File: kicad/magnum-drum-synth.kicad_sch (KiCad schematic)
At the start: 127 parts, among them J1 Piezo, J10 Conn_01x04_Header, J11 Conn_01x04_Socket, J12 Eurorack Mono Jack, J18 Eurorack Mono Jack, J2 Eurorack Mono Jack, J20 Conn_01x02_Socket, J21 Conn_01x02_Header, J22 Conn_01x02_Header, J23 Conn_01x02_Socket, J26 Eurorack Mono Jack, J3 Conn_01x04_Socket, J4 Conn_01x04_Header, J5 Conn_01x03_Header, J6 Conn_01x06_Header, J7 Conn_01x06_Socket, J8 Conn_01x06_Header, J9 Conn_01x06_Socket, Q1 2N3904, Q2 2N3904, Q3 2N3904, Q4 2N3904, Q5 2N3904, Q6 2N3906, Q7 2N3906, Q8 2N3906, Q9 2N3906, SW1 DPDT, U1 CD4093, U2 TL072, U3 TL072, U4 TL074, U7 LM13700

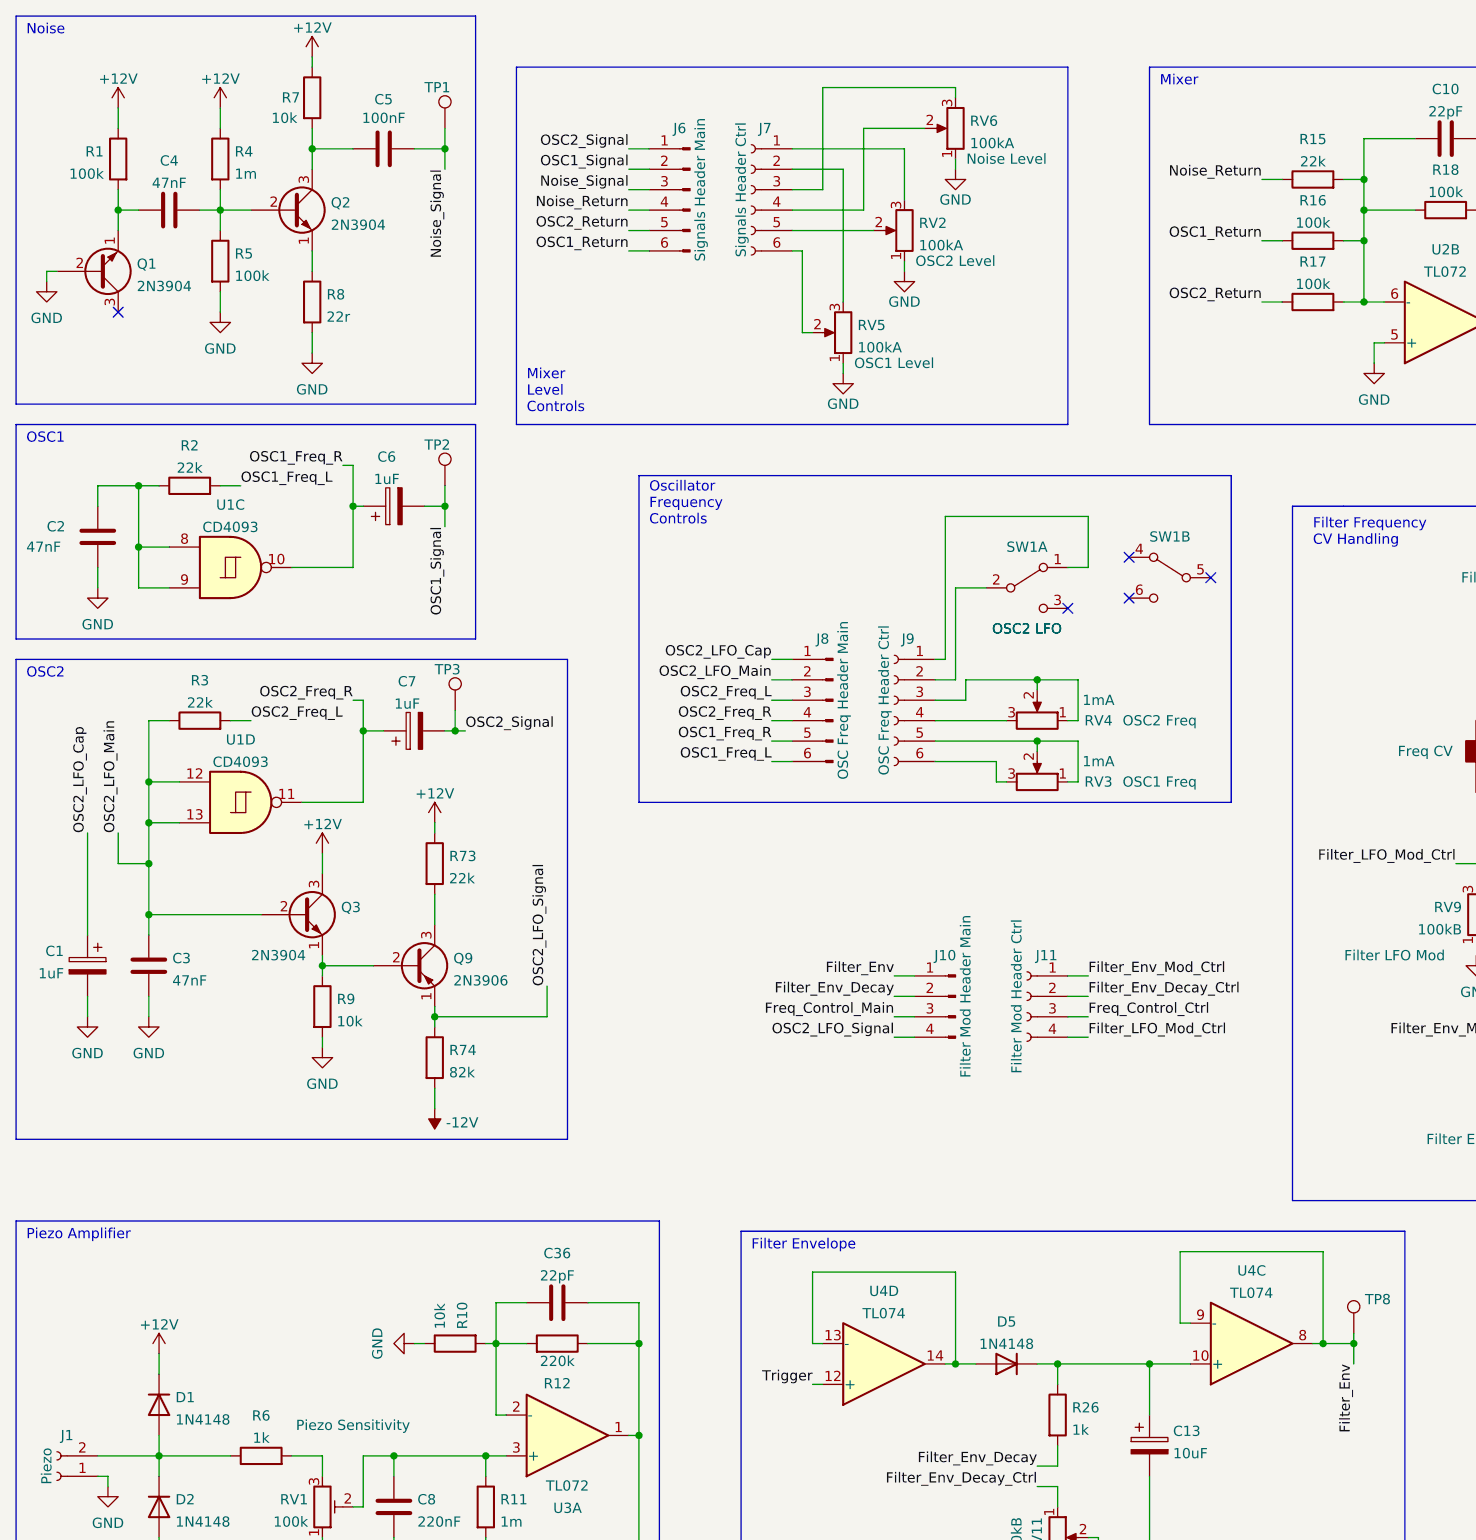
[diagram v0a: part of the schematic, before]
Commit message: Tweaking schematic and bom values
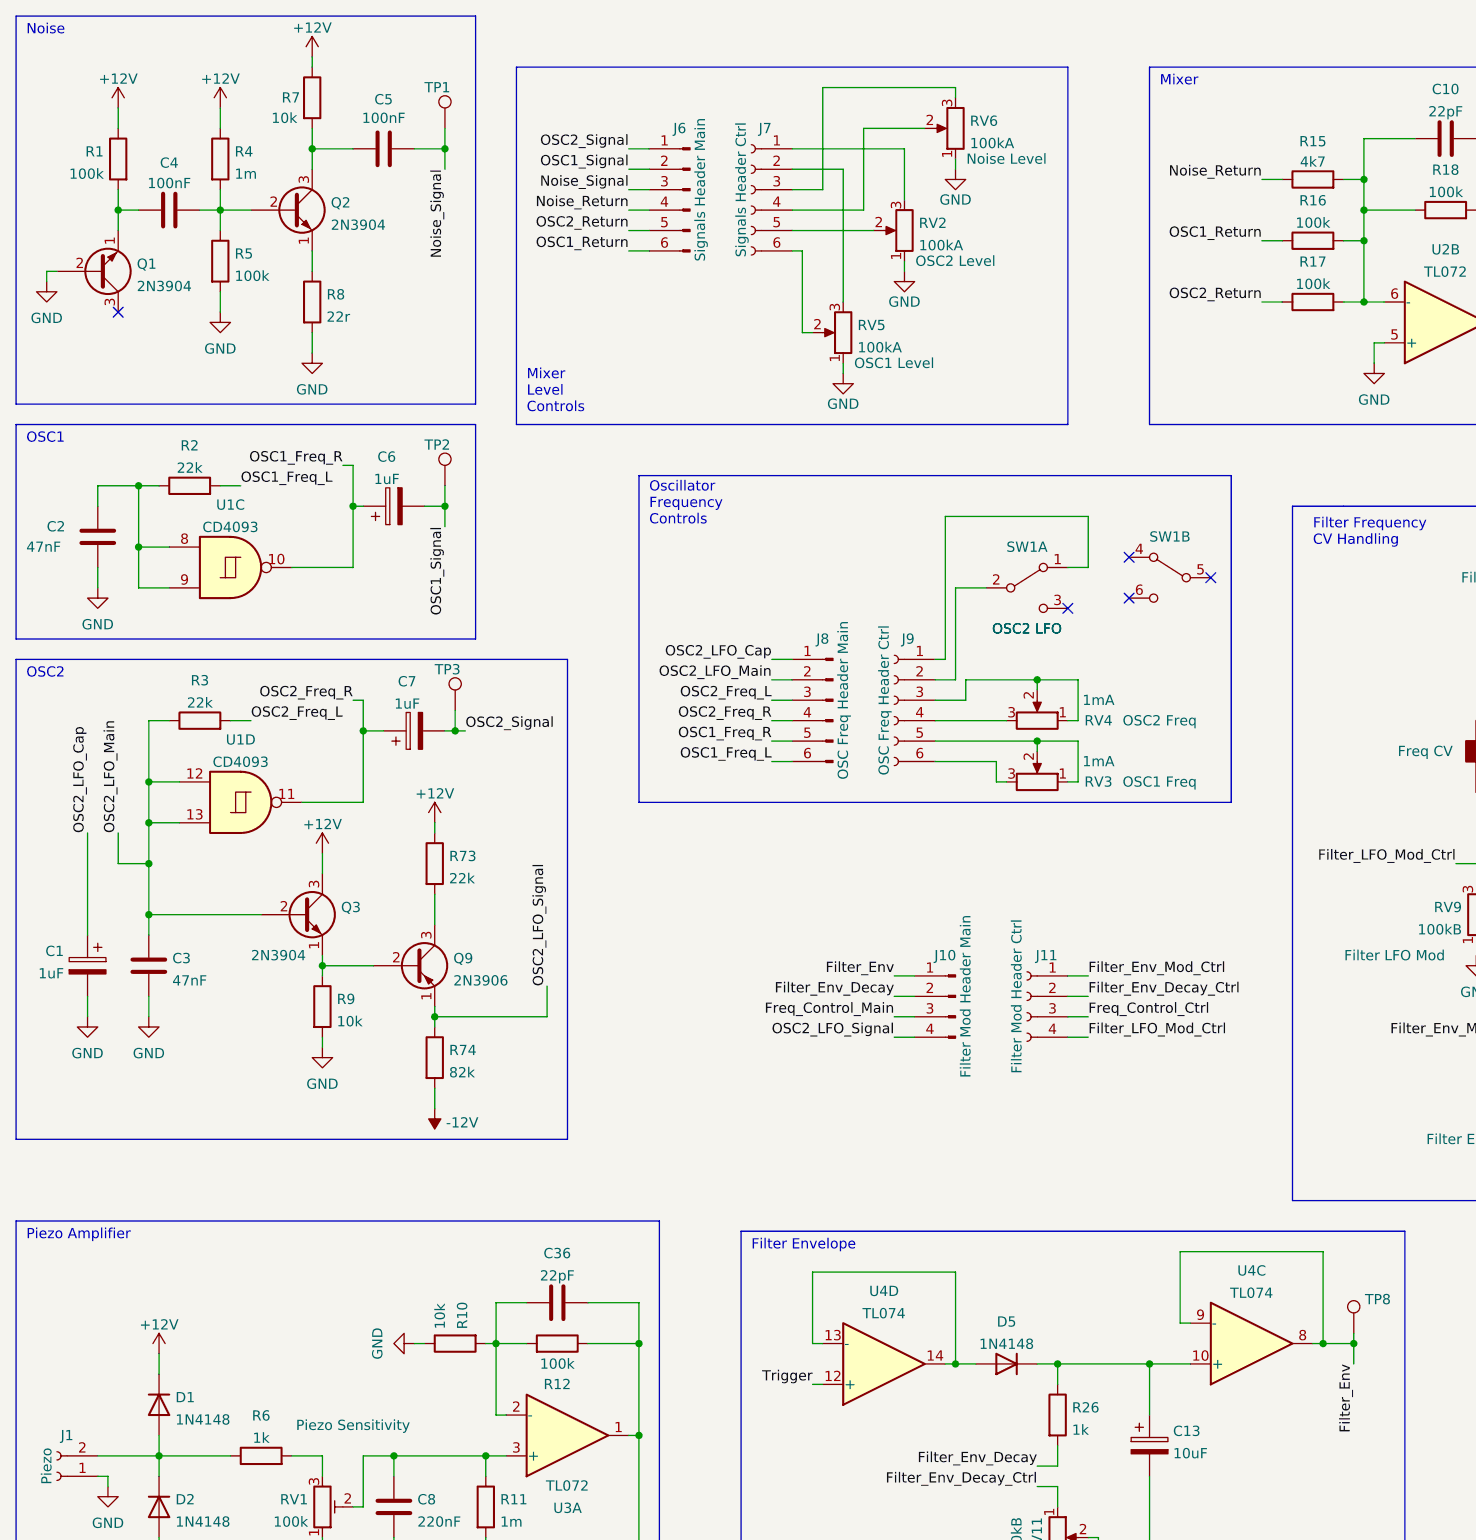
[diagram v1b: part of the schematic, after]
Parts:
- C4: value 47nF -> 100nF; Spec ceramic C0G -> ceramic X7R
- C8: Spec ceramic C0G -> ceramic X7R
- R12: value 220k -> 100k
- R15: value 22k -> 4k7
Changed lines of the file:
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@@
   (symbol (lib_id "Device:R") (at 175.26 34.29 90) (unit 1)
     (in_bom yes) (on_board yes) (fields_autoplaced)
-    (property "Reference" "R15" (id 0) (at 175.26 29.3075 90))
-    (property "Value" "22k" (id 1) (at 175.26 32.0826 90))
+    (property "Reference" "R15" (id 0) (at 175.26 29.5742 90))
+    (property "Value" "4k7" (id 1) (at 175.26 32.1111 90))
     (property "Footprint" "rumblesan-standard-parts:R_Axial_DIN0207_L6.3mm_D2.5mm_P10.16mm_Horizontal" (id 2) (at 175.26 36.068 90)
       (effects (font (size 1.27 1.27)) hide)
@@
   (symbol (lib_id "Device:C") (at 33.02 38.1 90) (unit 1)
     (in_bom yes) (on_board yes) (fields_autoplaced)
-    (property "Reference" "C4" (id 0) (at 33.02 31.9745 90))
-    (property "Value" "47nF" (id 1) (at 33.02 34.7496 90))
+    (property "Reference" "C4" (id 0) (at 33.02 32.2412 90))
+    (property "Value" "100nF" (id 1) (at 33.02 34.7781 90))
     (property "Footprint" "rumblesan-standard-parts:C_Rect_L7.0mm_W3.5mm_P5.00mm" (id 2) (at 36.83 37.1348 0)
       (effects (font (size 1.27 1.27)) hide)
@@
       (effects (font (size 1.27 1.27)) hide)
     )
-    (property "Spec" "ceramic C0G" (id 4) (at 33.02 38.1 0)
+    (property "Spec" "ceramic X7R" (id 4) (at 33.02 38.1 0)
       (effects (font (size 1.27 1.27)) hide)
     )
@@
       (effects (font (size 1.27 1.27)) hide)
     )
-    (property "Spec" "ceramic C0G" (id 4) (at 60.96 199.39 0)
+    (property "Spec" "ceramic X7R" (id 4) (at 60.96 199.39 0)
       (effects (font (size 1.27 1.27)) hide)
     )
@@
   )
   (symbol (lib_id "Device:R") (at 81.28 179.07 270) (mirror x) (unit 1)
-    (in_bom yes) (on_board yes) (fields_autoplaced)
-    (property "Reference" "R12" (id 0) (at 81.28 184.0525 90))
-    (property "Value" "220k" (id 1) (at 81.28 181.2774 90))
+    (in_bom yes) (on_board yes)
+    (property "Reference" "R12" (id 0) (at 81.28 184.15 90))
+    (property "Value" "100k" (id 1) (at 81.28 181.61 90))
     (property "Footprint" "rumblesan-standard-parts:R_Axial_DIN0207_L6.3mm_D2.5mm_P10.16mm_Horizontal" (id 2) (at 81.28 180.848 90)
       (effects (font (size 1.27 1.27)) hide)
@@
     )
     (path "/8591861f-2b7e-410e-8cfd-e20f7fcb6cbb"
-      (reference "C4") (unit 1) (value "47nF") (footprint "rumblesan-standard-parts:C_Rect_L7.0mm_W3.5mm_P5.00mm")
+      (reference "C4") (unit 1) (value "100nF") (footprint "rumblesan-standard-parts:C_Rect_L7.0mm_W3.5mm_P5.00mm")
     )
     (path "/0de452c1-c2d3-4d1a-b78a-15cceb3751d2"
@@
     )
     (path "/ad4c3087-473c-478a-8ad4-a1491b332c93/8e05464c-6ddb-45f0-a810-9a3b853897d8"
-      (reference "C21") (unit 1) (value "1uF") (footprint "rumblesan-standard-parts:CP_Radial_D5.0mm_P2.00mm")
+      (reference "C21") (unit 1) (value "10uF") (footprint "rumblesan-standard-parts:CP_Radial_D5.0mm_P2.00mm")
     )
     (path "/ad4c3087-473c-478a-8ad4-a1491b332c93/09fde542-3167-43f5-a315-cf966de10fd0"
-      (reference "C22") (unit 1) (value "1uF") (footprint "rumblesan-standard-parts:CP_Radial_D5.0mm_P2.00mm")
+      (reference "C22") (unit 1) (value "10uF") (footprint "rumblesan-standard-parts:CP_Radial_D5.0mm_P2.00mm")
     )
     (path "/ad4c3087-473c-478a-8ad4-a1491b332c93/e7127e9e-59ba-43a9-9501-cbea73a5bb0a"
@@
     )
     (path "/963dd436-ddf3-4162-9f66-c28717ca731d"
-      (reference "R12") (unit 1) (value "220k") (footprint "rumblesan-standard-parts:R_Axial_DIN0207_L6.3mm_D2.5mm_P10.16mm_Horizontal")
+      (reference "R12") (unit 1) (value "100k") (footprint "rumblesan-standard-parts:R_Axial_DIN0207_L6.3mm_D2.5mm_P10.16mm_Horizontal")
     )
     (path "/551bcd8e-03fa-4a5d-a22b-e038948336fc"
@@
     )
     (path "/33c83fc5-c4d0-450d-8557-408764e81e50"
-      (reference "R15") (unit 1) (value "22k") (footprint "rumblesan-standard-parts:R_Axial_DIN0207_L6.3mm_D2.5mm_P10.16mm_Horizontal")
+      (reference "R15") (unit 1) (value "4k7") (footprint "rumblesan-standard-parts:R_Axial_DIN0207_L6.3mm_D2.5mm_P10.16mm_Horizontal")
     )
     (path "/2eeac2dd-822d-48a2-8f8a-2fe3eb0d1b17"
@@
     )
     (path "/32f36dff-8662-485b-aca6-8ee96ddb3fbd/06d71e33-f77c-4bc4-8a4f-6532c1f037b7"
-      (reference "R71") (unit 1) (value "33k") (footprint "rumblesan-standard-parts:R_Axial_DIN0207_L6.3mm_D2.5mm_P10.16mm_Horizontal")
+      (reference "R71") (unit 1) (value "68k") (footprint "rumblesan-standard-parts:R_Axial_DIN0207_L6.3mm_D2.5mm_P10.16mm_Horizontal")
     )
     (path "/32f36dff-8662-485b-aca6-8ee96ddb3fbd/4a39f7d1-4843-4924-b280-b77be7d7ddd6"
-      (reference "R72") (unit 1) (value "10k") (footprint "rumblesan-standard-parts:R_Axial_DIN0207_L6.3mm_D2.5mm_P10.16mm_Horizontal")
+      (reference "R72") (unit 1) (value "33k") (footprint "rumblesan-standard-parts:R_Axial_DIN0207_L6.3mm_D2.5mm_P10.16mm_Horizontal")
     )
     (path "/c98fd5d1-af33-4d9b-9a1e-6ae175673044"

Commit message: Final tweaks to rev 4
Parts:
- removed J1: Piezo, Connector_PinHeader_2.54mm:PinHeader_1x02_P2.54mm_Vertical, symbol Connector:Conn_01x02_Female
- added C11: 10nF, rumblesan-standard-parts:C_Rect_L7.0mm_W3.5mm_P5.00mm, symbol Device:C
- added MK1: Piezo, Connector_PinHeader_2.54mm:PinHeader_1x02_P2.54mm_Vertical, symbol rumblesan-standard-parts:Piezo
- added R75: 100k, rumblesan-standard-parts:R_Axial_DIN0207_L6.3mm_D2.5mm_P10.16mm_Horizontal, symbol Device:R
- R12: value 100k -> 33k
- R37: value 4k3 -> 4k7
- R42: value 33k -> 47k
- RV10, RV11, RV12, RV7, RV8, RV9: footprint rumblesan-standard-parts:Potentiometer_Alpha_RD901F-40-00D_Single_Vertical -> rumblesan-standard-parts:Potentiometer_Alpha_RD901F-40-00D_Single_Vertical_CircularHoles
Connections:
- net GND: now also C11.1, MK1.1 (-)
- net at D3.1 (K), D4.1 (K), TP4.1: now also R75.1; no longer Q4.2 (B)
- net at D1.2 (A), D2.1 (K), R6.1: now also MK1.2 (+)
- new net: C11.2, Q4.2 (B), R75.2
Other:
- moved on the sheet: C9, D1, D2, Q4, R13, R14, R6, TP5, U1A, U1B

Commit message: Final export of everything for rev4
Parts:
- C11: Spec ceramic X7R -> ceramic C0G
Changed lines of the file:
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@@
     (pin "1")
   )
-  (symbol (lib_id "Device:C") (at 92.71 262.89 180) (unit 1)
-    (in_bom yes) (on_board yes)
-    (property "Reference" "C11" (id 0) (at 86.36 262.89 0)
-      (effects (font (size 1.27 1.27)) (justify right))
-    )
-    (property "Value" "10nF" (id 1) (at 83.82 265.43 0)
-      (effects (font (size 1.27 1.27)) (justify right))
-    )
-    (property "Footprint" "rumblesan-standard-parts:C_Rect_L7.0mm_W3.5mm_P5.00mm" (id 2) (at 91.7448 259.08 0)
-      (effects (font (size 1.27 1.27)) hide)
-    )
-    (property "Datasheet" "~" (id 3) (at 92.71 262.89 0)
-      (effects (font (size 1.27 1.27)) hide)
-    )
-    (property "Spec" "ceramic X7R" (id 4) (at 92.71 262.89 0)
-      (effects (font (size 1.27 1.27)) hide)
-    )
-    (property "Tolerance" "5%" (id 5) (at 92.71 262.89 0)
-      (effects (font (size 1.27 1.27)) hide)
-    )
-    (pin "1")
-    (pin "2")
-  )
   (symbol (lib_id "Device:R_Potentiometer") (at 204.47 88.9 0) (mirror x) (unit 1)
     (in_bom yes) (on_board yes)
@@
     (pin "7")
   )
+  (symbol (lib_id "Device:C") (at 92.71 262.89 180) (unit 1)
+    (in_bom yes) (on_board yes) (fields_autoplaced)
+    (property "Reference" "C11" (id 0) (at 95.631 262.0553 0)
+      (effects (font (size 1.27 1.27)) (justify right))
+    )
+    (property "Value" "10nF" (id 1) (at 95.631 264.5922 0)
+      (effects (font (size 1.27 1.27)) (justify right))
+    )
+    (property "Footprint" "rumblesan-standard-parts:C_Rect_L7.0mm_W3.5mm_P5.00mm" (id 2) (at 91.7448 259.08 0)
+      (effects (font (size 1.27 1.27)) hide)
+    )
+    (property "Datasheet" "~" (id 3) (at 92.71 262.89 0)
+      (effects (font (size 1.27 1.27)) hide)
+    )
+    (property "Spec" "ceramic C0G" (id 4) (at 92.71 262.89 0)
+      (effects (font (size 1.27 1.27)) hide)
+    )
+    (property "Tolerance" "5%" (id 5) (at 92.71 262.89 0)
+      (effects (font (size 1.27 1.27)) hide)
+    )
+    (pin "1")
+    (pin "2")
+  )
   (symbol (lib_id "Switch:SW_DPDT_x2") (at 157.48 83.82 0) (mirror y) (unit 2)
     (in_bom yes) (on_board yes)
@@
       (reference "C10") (unit 1) (value "22pF") (footprint "rumblesan-standard-parts:C_Rect_L7.0mm_W3.5mm_P5.00mm")
     )
-    (path "/208b7b28-15f4-4d91-86ff-007b76285e4e"
+    (path "/4c1618c7-728a-45ee-8f44-b3ec259b0cad"
       (reference "C11") (unit 1) (value "10nF") (footprint "rumblesan-standard-parts:C_Rect_L7.0mm_W3.5mm_P5.00mm")
     )

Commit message: Fixing trigger piezo normalling
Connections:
- net GND: now also J2.S (Sleeve); no longer J2.TN (Tip_normalize)
- net at J3.2 (Pin_2): now also J2.TN (Tip_normalize); no longer J2.S (Sleeve)
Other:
- moved on the sheet: J2
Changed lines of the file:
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@@
     (pin "2")
   )
-  (symbol (lib_id "Eurorack_Hardware:Eurorack Mono Jack") (at 24.13 256.54 180) (unit 1)
+  (symbol (lib_id "Eurorack_Hardware:Eurorack Mono Jack") (at 24.13 254 0) (mirror y) (unit 1)
     (in_bom yes) (on_board yes)
-    (property "Reference" "J2" (id 0) (at 22.86 250.19 0)
+    (property "Reference" "J2" (id 0) (at 22.86 260.35 0)
       (effects (font (size 1.27 1.27)) (justify right))
     )
-    (property "Value" "Eurorack Mono Jack" (id 1) (at 24.13 261.62 0)
+    (property "Value" "Eurorack Mono Jack" (id 1) (at 24.13 248.92 0)
       (effects (font (size 1.27 1.27)) hide)
     )
-    (property "Footprint" "rumblesan-standard-parts:Jack_3.5mm_QingPu_WQP-PJ398SM_Vertical" (id 2) (at 22.86 247.65 0)
+    (property "Footprint" "rumblesan-standard-parts:Jack_3.5mm_QingPu_WQP-PJ398SM_Vertical" (id 2) (at 22.86 262.89 0)
       (effects (font (size 1.27 1.27)) hide)
     )
@@
       (effects (font (size 1.27 1.27)) hide)
     )
-    (property "Name" "Trig In" (id 4) (at 24.13 262.89 0))
-    (property "mpn" "WQP-WQP518MA" (id 5) (at 24.13 250.19 0)
+    (property "Name" "Trig In" (id 4) (at 24.13 247.65 0))
+    (property "mpn" "WQP-WQP518MA" (id 5) (at 24.13 260.35 0)
       (effects (font (size 1.27 1.27)) hide)
     )

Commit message: Rejigging interconnects
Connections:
- net OSC2_LFO_Cap_Ctrl: now reaches J9.1 (Pin_1), SW1.1 (A)
- net OSC2_LFO_Main_Ctrl: now reaches J9.2 (Pin_2), SW1.2 (B)
- net OSC2_Freq_L_Ctrl: now reaches J9.3 (Pin_3), RV4.1, RV4.2
- net OSC2_Freq_R_Ctrl: now reaches J9.4 (Pin_4), RV4.3
- net OSC1_Freq_R_Ctrl: now reaches J9.5 (Pin_5), RV3.1, RV3.2
- net OSC1_Freq_L_Ctrl: now reaches J9.6 (Pin_6), RV3.3
- net Res_Amount_Ctrl: now reaches J23.2 (Pin_2), RV12.2
- net Res_Top_Ctrl: now reaches J23.1 (Pin_1), RV12.3
- net Noise_Return_Ctrl: now reaches J7.4 (Pin_4), RV6.2
- net Noise_Signal_Ctrl: now reaches J7.3 (Pin_3), RV6.3
- net OSC1_Return_Ctrl: now reaches J7.6 (Pin_6), RV5.2
- net OSC1_Signal_Ctrl: now reaches J7.2 (Pin_2), RV5.3
- net PIEZO_CTRL: now reaches C36.2, J3.1 (Pin_1), R12.1, U3.1
- net TRIG_IN_MAIN: now reaches D4.2 (A), J4.3 (Pin_3)
- net PIEZO_NORMAL_CTRL: now reaches J2.TN (Tip_normalize), J3.2 (Pin_2)
- net TRIG_IN_CTRL: now reaches J2.T (Tip), J3.3 (Pin_3)
- net AMP_DECAY_CV_MAIN: now reaches J21.1 (Pin_1), R30.1
- net AMP_DECAY_MAIN: now reaches J21.2 (Pin_2), R27.2
- net AMP_DECAY_CTRL: now reaches J20.2 (Pin_2), R25.1, RV10.2
- net AMP_DECAY_CV_CTRL: now reaches J18.T (Tip), J20.1 (Pin_1)
- net PIEZO_MAIN: now reaches J4.1 (Pin_1), J5.2 (Pin_2)
- net PIEZO_NORMAL_MAIN: now reaches J4.2 (Pin_2), J5.3 (Pin_3)
- net OSC2_Return_Ctrl: now reaches J7.5 (Pin_5), RV2.2
- net OSC2_Signal_Ctrl: now reaches J7.1 (Pin_1), RV2.3
- net Final_Output_Ctrl renamed FINAL_OUTPUT_CTRL
- net Final_Output_Main renamed FINAL_OUTPUT_MAIN
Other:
- moved on the sheet: C11, C12, C14, C16, C9, D3, D4, D6, J10, J11, J12, J18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

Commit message: Moving mixer opamp to front board
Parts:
- removed U3: TL072, rumblesan-standard-parts:DIP-8_W7.62mm_Socket, symbol Amplifier_Operational:TL072
- added U3: TL074, rumblesan-standard-parts:DIP-14_W7.62mm_Socket, symbol Amplifier_Operational:TL074
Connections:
- net Freq_Control_Ctrl: now also U3.1
- net GND: now also U3.12 (+), U3.3 (+), U3.5 (+)
- net PIEZO_CTRL: now also U3.8
- net at C12.1, R19.2, R20.2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: now also U3.2 (-)
- net at C10.1, R15.2, R16.2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: now also U3.13 (-); no longer U2.6 (-)
- net at C8.2, R11.1, RV1.2: now also U3.10 (+)
- net at C36.1, R10.2, R12.2: now also U3.9 (-)
- net Filter/Input renamed MIX_RETURN_CTRL
- net MIX_RETURN_CTRL: now also J7.4 (Pin_4), U3.14; no longer TP6.1, U2.7
- net Noise_Return: no longer names the net of R15.1
- net Noise_Return: now also RV6.2; no longer J6.4 (Pin_4)
- removed net Noise_Return_Ctrl: J7.4 (Pin_4), RV6.2
- net OSC1_Return: no longer names the net of J6.6 (Pin_6)
- net OSC1_Return: no longer R16.1
- net OSC1_Return_Ctrl: no longer names the net of RV5.2
- net OSC1_Return_Ctrl: now also R16.1; no longer J7.6 (Pin_6)
- net OSC2_Return: no longer names the net of J6.5 (Pin_5)
- net OSC2_Return: no longer R17.1
- net OSC2_Return_Ctrl: no longer names the net of RV2.2
- net OSC2_Return_Ctrl: now also R17.1; no longer J7.5 (Pin_5)
- new net: U2.6 (-), U2.7
- new net: U3.6 (-), U3.7
- new net MIX_RETURN_MAIN: J6.4 (Pin_4), TP6.1
- no-connect marks 9 -> 13
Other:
- note removed: "Mixer Level Controls"
- moved on the sheet: C10, R15, R16, R17, R18, RV2, RV5, RV6, TP6, U2B
